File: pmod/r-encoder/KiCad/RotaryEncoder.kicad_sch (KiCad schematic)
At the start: 15 parts, among them J1 Conn_01x06, U1 PEC11R-4325F-S0012

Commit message: fix: connectors
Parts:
- J1: footprint Connector_PinHeader_2.54mm:PinHeader_1x06_P2.54mm_Vertical -> Connector_PinHeader_2.54mm:PinHeader_1x06_P2.54mm_Horizontal
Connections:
- net A: now also J1.4 (Pin_4); no longer J1.1 (Pin_1)
- net B: now also J1.3 (Pin_3); no longer J1.2 (Pin_2)
- net BTN: now also J1.2 (Pin_2); no longer J1.3 (Pin_3)
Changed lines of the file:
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@@
-		)
-	)
-	(global_label "A"
-		(shape input)
-		(at 27.94 44.45 0)
-		(fields_autoplaced yes)
-		(effects
-			(font
-				(size 1.27 1.27)
-			)
-			(justify left)
-		)
-		(property "Intersheetrefs" "${INTERSHEET_REFS}"
-			(at 32.0138 44.45 0)
-			(effects
-				(font
-					(size 1.27 1.27)
-				)
-				(justify left)
-				(hide yes)
-			)
 		)
 	)
 	(global_label "B"
 		(shape input)
-		(at 27.94 46.99 0)
+		(at 27.94 49.53 0)
 		(fields_autoplaced yes)
 		(effects
@@
 		)
 		(property "Intersheetrefs" "${INTERSHEET_REFS}"
-			(at 32.1952 46.99 0)
+			(at 32.1952 49.53 0)
 			(effects
 				(font
@@
 	(global_label "BTN"
 		(shape input)
-		(at 27.94 49.53 0)
+		(at 27.94 46.99 0)
 		(fields_autoplaced yes)
 		(effects
@@
 		)
 		(property "Intersheetrefs" "${INTERSHEET_REFS}"
-			(at 34.4933 49.53 0)
+			(at 34.4933 46.99 0)
 			(effects
 				(font
@@
 				)
 				(justify right)
+				(hide yes)
+			)
+		)
+	)
+	(global_label "A"
+		(shape input)
+		(at 27.94 52.07 0)
+		(fields_autoplaced yes)
+		(effects
+			(font
+				(size 1.27 1.27)
+			)
+			(justify left)
+		)
+		(property "Intersheetrefs" "${INTERSHEET_REFS}"
+			(at 32.0138 52.07 0)
+			(effects
+				(font
+					(size 1.27 1.27)
+				)
+				(justify left)
 				(hide yes)
 			)
@@
 			)
 		)
-		(property "Footprint" "Connector_PinHeader_2.54mm:PinHeader_1x06_P2.54mm_Vertical"
+		(property "Footprint" "Connector_PinHeader_2.54mm:PinHeader_1x06_P2.54mm_Horizontal"
 			(at 22.86 49.53 0)
 			(effects

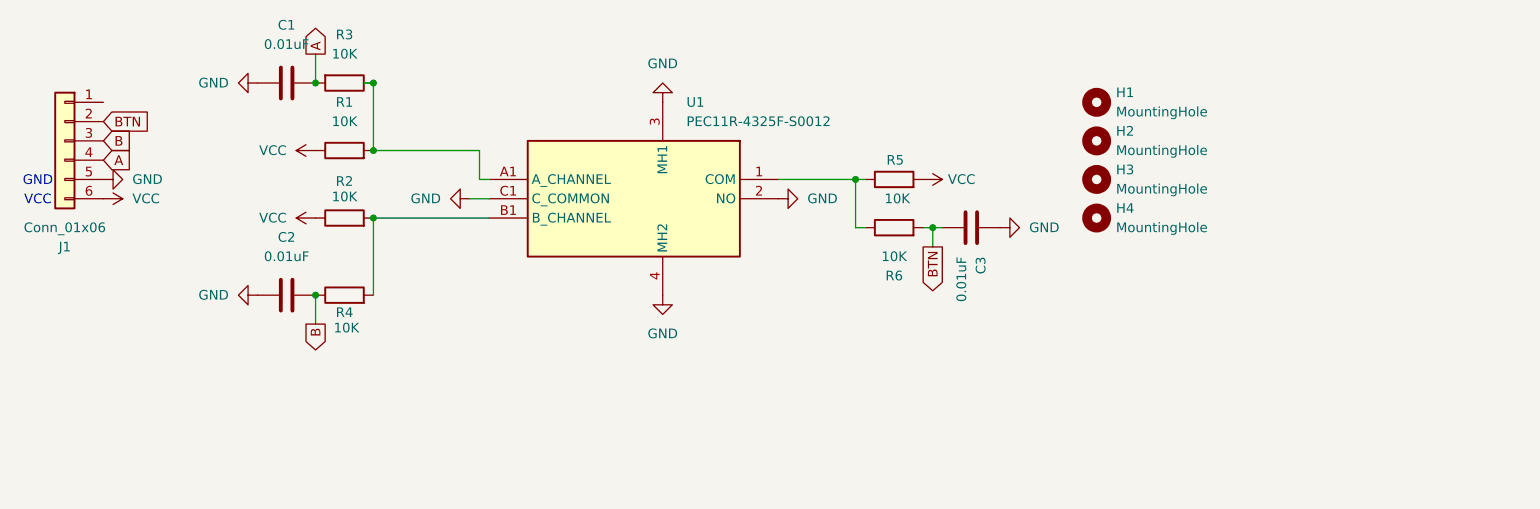
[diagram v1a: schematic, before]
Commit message: fix: prepare all board for manufacturing
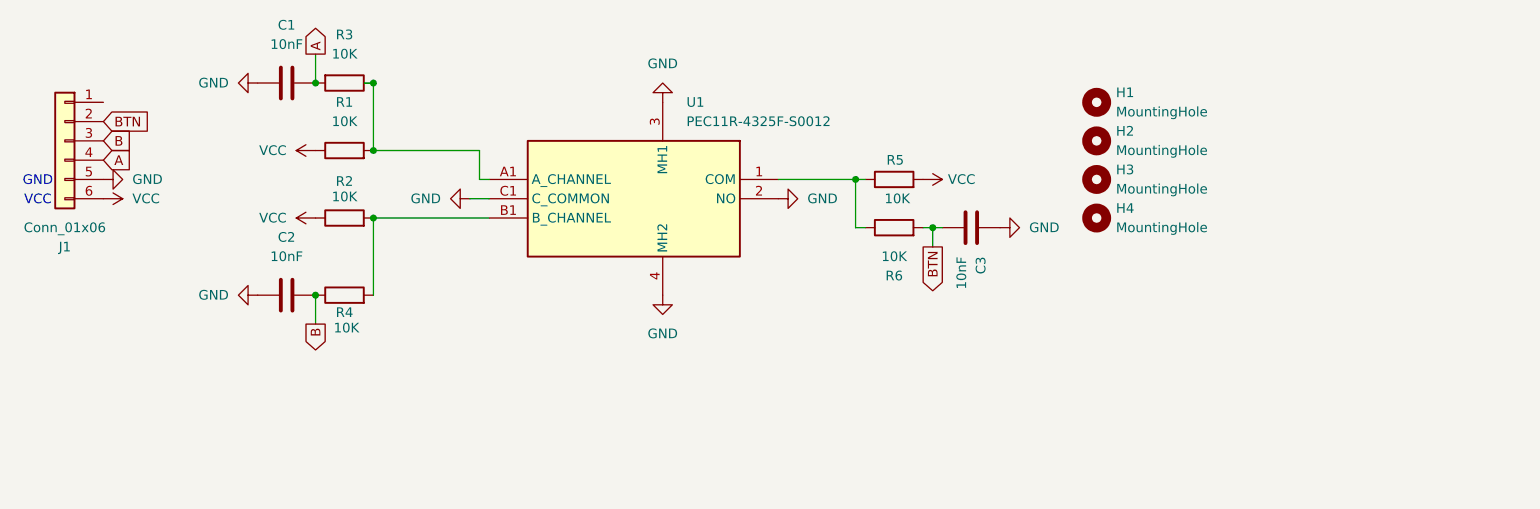
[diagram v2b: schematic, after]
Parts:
- C1, C2, C3: value 0.01uF -> 10nF

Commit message: docs: add images, fix docs
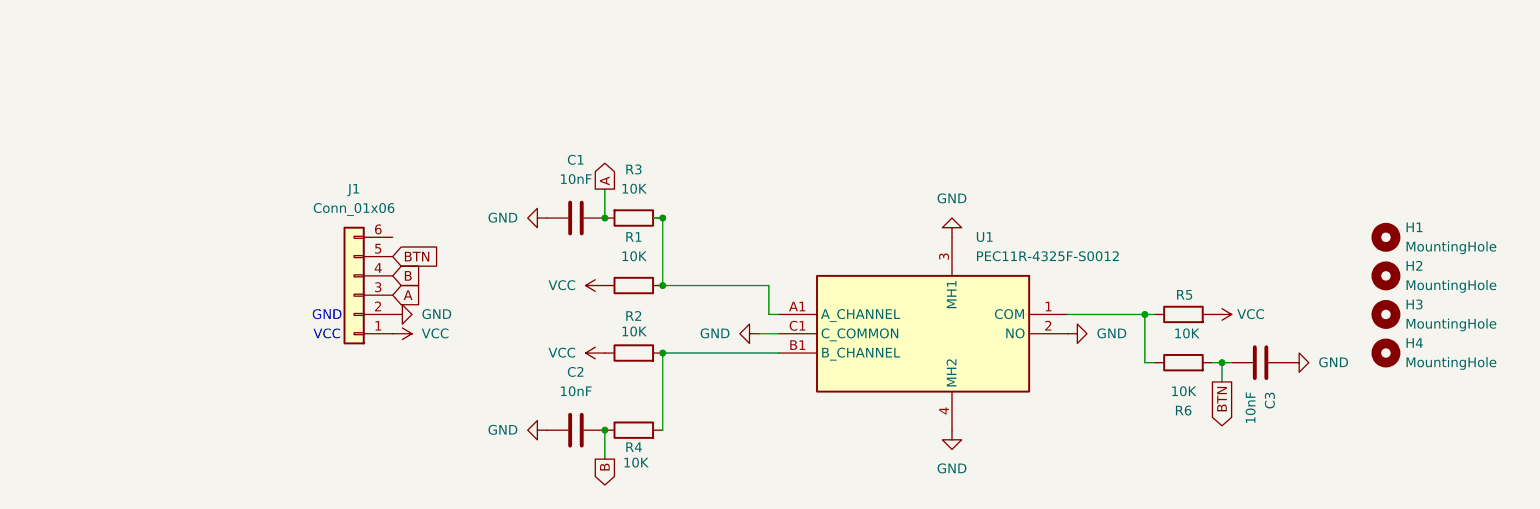
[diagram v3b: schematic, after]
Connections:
- net A: now also J1.3 (Pin_3); no longer J1.4 (Pin_4)
- net B: now also J1.4 (Pin_4); no longer J1.3 (Pin_3)
- net BTN: now also J1.5 (Pin_5); no longer J1.2 (Pin_2)
- net GND: now also J1.2 (Pin_2); no longer J1.5 (Pin_5)
- net VCC: now also J1.1 (Pin_1); no longer J1.6 (Pin_6)
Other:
- moved on the sheet: C1, C2, C3, H1, H2, H3, H4, R1, R2, R3, R4, R5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
